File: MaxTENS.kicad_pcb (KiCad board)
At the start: 2 copper layers, 50.8 x 70.1 mm, 74 parts, among them IC1 ESP32-WROOM-32E-N8, J2 54-00170, J3 54-00170, J4 Conn_01x12, J5 20021121-00010C4LF, J6 Conn_01x02_Pin, Q1 PMV37ENEAR, Q16 NPN, Q17 PNP, Q18 NPN, Q19 NPN, Q2 NPN, Q20 PNP, Q21 NPN, Q3 NPN, Q4 NPN, Q5 PNP, Q6 NPN, Q7 NPN, Q8 PNP, Q9 NPN, U1 ADA4522-2ARMZ-R7, U2 MCP4232-503E/UN, U3 MCP73811T-420I/OT, U4 NCP176AMX330TCG

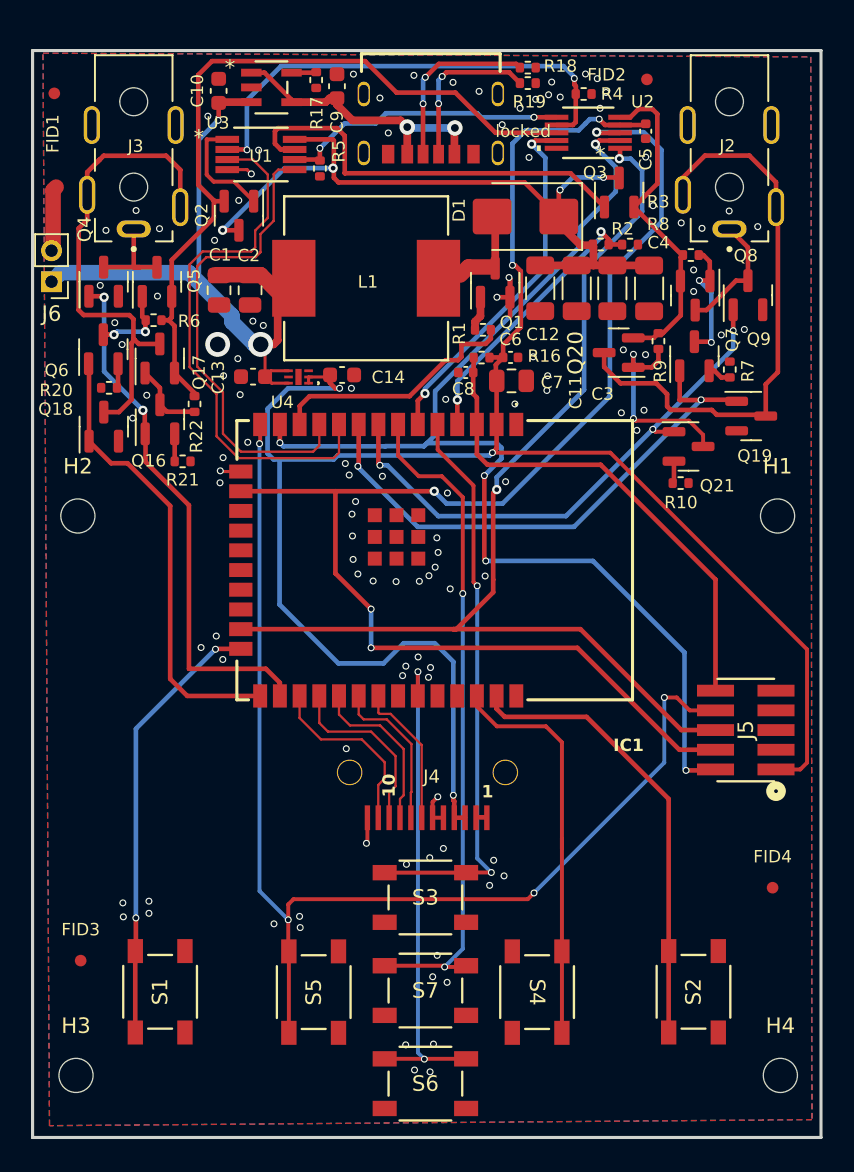
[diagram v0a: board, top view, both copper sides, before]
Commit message: version 2 with 0.8mm thickness
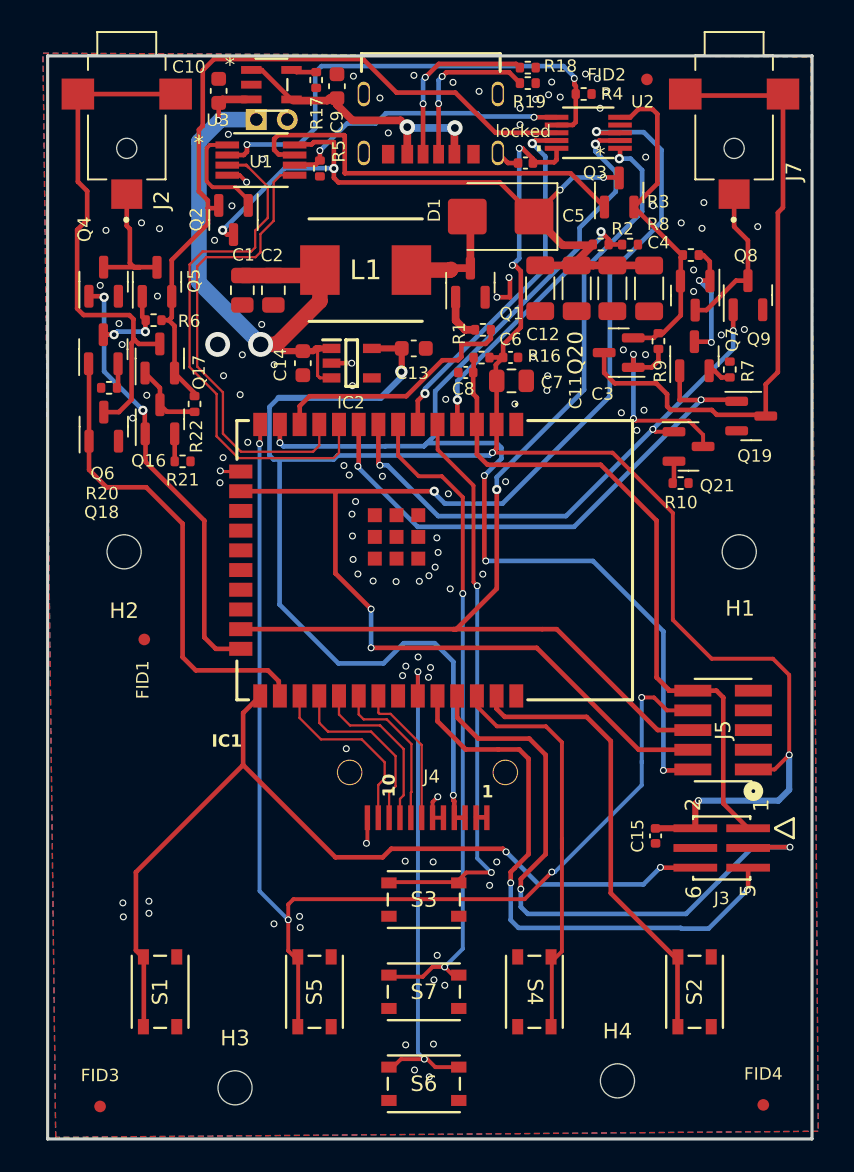
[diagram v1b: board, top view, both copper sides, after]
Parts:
- removed U4: NCP176AMX330TCG, Library:XDFN6_711AT_ONS
- added C15: 0.1u, Capacitor_SMD:C_0402_1005Metric, F.Cu at (238.0, 90.6)
- added IC2: AP7366-33W5-7, Library:SOT95P285X130-5N, F.Cu at (218.4, 60.1)
- added J7: PJ-040-SMT-TR, Library:CUI_PJ-040-SMT-TR, F.Cu at (243.1, 44.3)
- J2: value 54-00170 -> PJ-040-SMT-TR; footprint Library:TENSILITY_54-00170 -> Library:CUI_PJ-040-SMT-TR
- J3: value 54-00170 -> 20021121-00006C4LF; footprint Library:TENSILITY_54-00170 -> Library:CONN_20021121-00006C4LF_AMP
- J6: moved to B.Cu
- L1: value 33uH -> 10uH; footprint Library:IND_104CDM_SUM -> Library:INDPM7366X300N
- S1, S2, S3, S4, S5, S6, S7: value PTS647SM38SMTR2LFS -> PTS815 SJM 250 SMTR LFS; footprint Library:SW_PTS647SM38SMTR2LFS_CNK -> Library:SW4_PTS815 SJM 250 SMTR LFS_CNK
- moved J3 59.1 mm to (242.3, 91.4), turned to 90 degrees
- moved J2 38.9 mm to (203.9, 44.3), turned to -90 degrees
- moved FID1 35.7 mm to (205.1, 78.0)
- moved J6 16.8 mm to (212.3, 44.5), turned to -90 degrees
- moved FID4 14.0 mm to (245.0, 108.0)
- moved C13 10.5 mm to (222.4, 59.2), turned to 0 degrees
- moved H4 10.5 mm to (235.6, 106.4)
- moved H3 10.3 mm to (210.9, 106.9)
- moved FID3 9.48 mm to (202.2, 108.1)
- moved C5 8.02 mm to (229.7, 47.2), turned to 180 degrees
- moved H2 3.77 mm to (203.8, 72.3)
- moved H1 3.38 mm to (243.4, 72.3)
- moved C14 2.64 mm to (215.3, 60.1), turned to -90 degrees
- moved D1 1.60 mm to (228.1, 50.7)
- moved Q1 1.60 mm to (226.1, 55.0)
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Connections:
- C13 pad 1: +BATT -> +3.3V
- C14 pad 1: +3.3V -> +BATT
- IC1 pad 24: /MCU/CH1_BTN -> /ElectrodeChannels/CH1_1
- IC1 pad 25: /ElectrodeChannels/CH1_2 -> /MCU/CH1_BTN
- IC1 pad 26: /ElectrodeChannels/CH1_1 -> /ElectrodeChannels/CH1_2
- IC1 pad 34: unconnected-(IC1-RXD0-Pad34) -> /MCU/RXD
- IC1 pad 35: unconnected-(IC1-TXD0-Pad35) -> /MCU/TXD
- U2 pad 10: GND -> +3.3V
- U2 pad 4: +3.3V -> GND
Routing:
- net /MCU/TXD: track 0.00 -> 40.6 mm, vias 0 -> 2
- net /MCU/RXD: track 0.00 -> 37.3 mm, vias 0 -> 2
- net /MCU/CH1_BTN: track 28.5 -> 58.1 mm
- net +3.3V: track 126.6 -> 140.2 mm, vias 5 -> 7
- net /MCU/EN: track 32.2 -> 43.8 mm
- net /ElectrodeChannels/CH1_1: track 34.3 -> 28.3 mm
- net GND: track 17.3 -> 13.3 mm, vias 114 -> 109
- net /ElectrodeChannels/CH2_N: track 37.0 -> 40.8 mm
- net +BATT: track 50.4 -> 47.4 mm
- net /ElectrodeChannels/CH1_P: track 6.29 -> 8.72 mm
- net /ElectrodeChannels/CH2_P: track 8.01 -> 10.0 mm
- net Net-(D1-A): track 5.56 -> 7.26 mm
- net /MCU/CS: track 70.5 -> 69.0 mm
- net VCC: track 47.7 -> 49.1 mm
- net /ElectrodeChannels/CH1_2: track 29.4 -> 30.7 mm
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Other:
- board size 50.8 x 70.1 mm -> 49.3 x 69.8 mm

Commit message: v3: removed digital potentiometer, added 8 discrete resistors and one GPIO expander
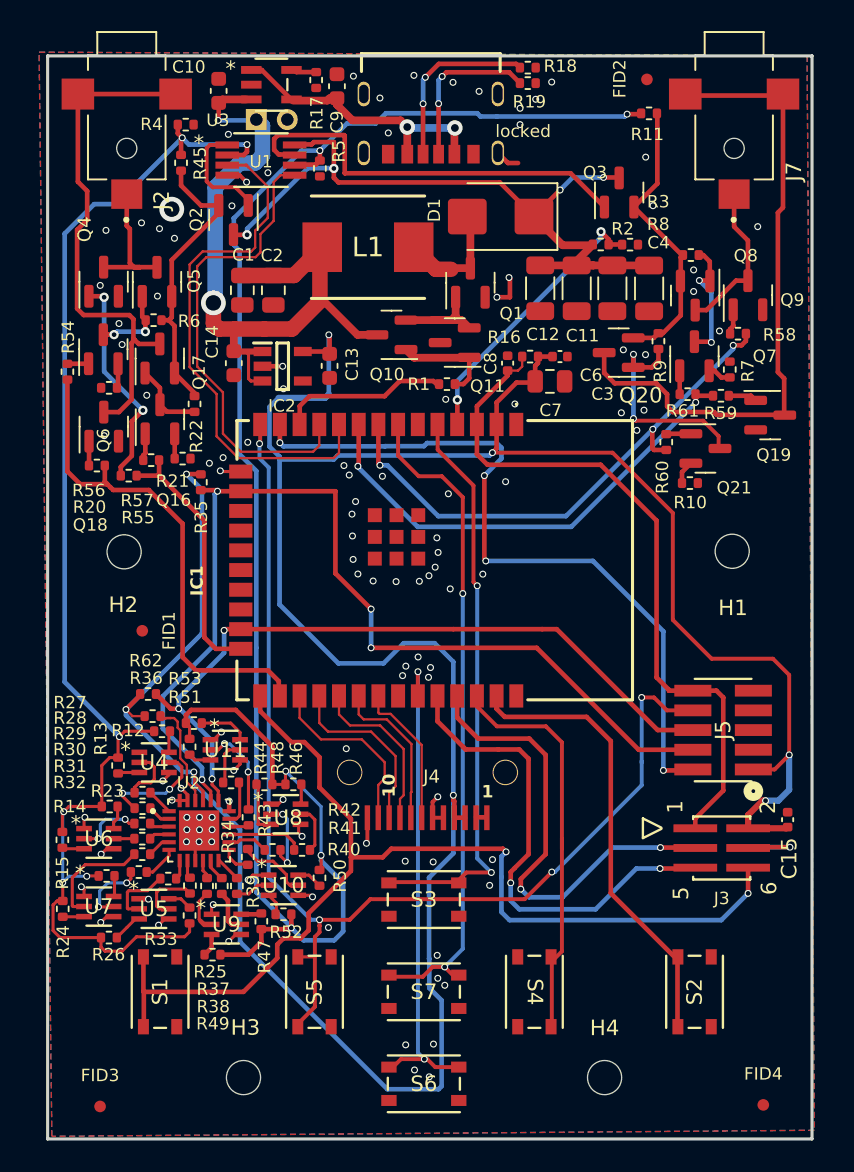
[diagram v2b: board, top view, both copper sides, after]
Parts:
- removed C5: 0.1u, Capacitor_SMD:C_0402_1005Metric
- added Q10: NPN, Package_TO_SOT_SMD:SOT-23, F.Cu at (221.0, 58.3)
- added Q11: PNP, Package_TO_SOT_SMD:SOT-23, F.Cu at (225.1, 58.8)
- added R11: 16k, Resistor_SMD:R_0402_1005Metric, F.Cu at (237.6, 44.0)
- added R12: 1M, Resistor_SMD:R_0402_1005Metric, F.Cu at (206.2, 83.9)
- added R13: 10k, Resistor_SMD:R_0402_1005Metric, F.Cu at (203.4, 86.1)
- added R14: 4.99k, Resistor_SMD:R_0402_1005Metric, F.Cu at (202.8, 88.7)
- added R15: 3.3k, Resistor_SMD:R_0402_1005Metric, F.Cu at (199.8, 90.9)
- added R23: 2.4k, Resistor_SMD:R_0402_1005Metric, F.Cu at (202.7, 93.2)
- added R24: 3.3k, Resistor_SMD:R_0402_1005Metric, F.Cu at (199.8, 95.3)
- added R25: 1.43k, Resistor_SMD:R_0402_1005Metric, F.Cu at (208.0, 95.8)
- added R26: 1.1k, Resistor_SMD:R_0402_1005Metric, F.Cu at (202.8, 97.2)
- added R27: 510, Resistor_SMD:R_0402_1005Metric, F.Cu at (205.0, 87.8)
- added R28: 510, Resistor_SMD:R_0402_1005Metric, F.Cu at (205.0, 88.8)
- added R29: 510, Resistor_SMD:R_0402_1005Metric, F.Cu at (204.9, 89.8)
- added R30: 510, Resistor_SMD:R_0402_1005Metric, F.Cu at (204.9, 90.8)
- added R31: 510, Resistor_SMD:R_0402_1005Metric, F.Cu at (204.9, 91.8)
- added R32: 510, Resistor_SMD:R_0402_1005Metric, F.Cu at (204.7, 93.0)
- added R33: 510, Resistor_SMD:R_0402_1005Metric, F.Cu at (206.6, 93.4)
- added R34: 510, Resistor_SMD:R_0402_1005Metric, F.Cu at (208.0, 93.8)
- added R35: 10k, Resistor_SMD:R_0402_1005Metric, F.Cu at (208.7, 67.8)
- added R36: 10k, Resistor_SMD:R_0402_1005Metric, F.Cu at (205.3, 81.5)
- added R37: 510, Resistor_SMD:R_0402_1005Metric, F.Cu at (209.1, 93.8)
- added R38: 510, Resistor_SMD:R_0402_1005Metric, F.Cu at (210.1, 93.8)
- added R39: 510, Resistor_SMD:R_0402_1005Metric, F.Cu at (211.1, 93.8)
- added R40: 510, Resistor_SMD:R_0402_1005Metric, F.Cu at (211.8, 92.0)
- added R41: 510, Resistor_SMD:R_0402_1005Metric, F.Cu at (213.3, 91.5)
- added R42: 510, Resistor_SMD:R_0402_1005Metric, F.Cu at (215.2, 91.5)
- added R43: 510, Resistor_SMD:R_0402_1005Metric, F.Cu at (211.8, 89.4)
- added R44: 510, Resistor_SMD:R_0402_1005Metric, F.Cu at (210.7, 87.2)
- added R45: 16k, Resistor_SMD:R_0402_1005Metric, F.Cu at (207.4, 47.2)
- added R46: 2.4k, Resistor_SMD:R_0402_1005Metric, F.Cu at (214.7, 87.3)
- added R47: 1M, Resistor_SMD:R_0402_1005Metric, F.Cu at (212.6, 96.1)
- added R48: 3.3k, Resistor_SMD:R_0402_1005Metric, F.Cu at (212.8, 87.3)
- added R49: 10k, Resistor_SMD:R_0402_1005Metric, F.Cu at (209.5, 98.3)
- added R50: 4.99k, Resistor_SMD:R_0402_1005Metric, F.Cu at (216.4, 93.3)
- added R51: 1.43k, Resistor_SMD:R_0402_1005Metric, F.Cu at (208.3, 83.3)
- added R52: 3.3k, Resistor_SMD:R_0402_1005Metric, F.Cu at (214.1, 95.7)
- added R53: 1.1k, Resistor_SMD:R_0402_1005Metric, F.Cu at (208.0, 84.9)
- added R54: 300, Resistor_SMD:R_0402_1005Metric, F.Cu at (200.1, 60.7)
- added R55: 300, Resistor_SMD:R_0402_1005Metric, F.Cu at (204.1, 67.4)
- added R56: 300, Resistor_SMD:R_0402_1005Metric, F.Cu at (202.0, 66.8)
- added R57: 300, Resistor_SMD:R_0402_1005Metric, F.Cu at (205.5, 66.4)
- added R58: 300, Resistor_SMD:R_0402_1005Metric, F.Cu at (243.3, 58.2)
- added R59: 300, Resistor_SMD:R_0402_1005Metric, F.Cu at (242.2, 62.2)
- added R60: 300, Resistor_SMD:R_0402_1005Metric, F.Cu at (238.7, 65.2)
- added R61: 300, Resistor_SMD:R_0402_1005Metric, F.Cu at (240.1, 62.1)
- added R62: 10k, Resistor_SMD:R_0402_1005Metric, F.Cu at (205.6, 82.9)
- added U10: 2N7002KDW_R1_00001, Library:SOT-363-6_2P2X1P35_ONS, F.Cu at (214.1, 93.8)
- added U11: 2N7002KDW_R1_00001, Library:SOT-363-6_2P2X1P35_ONS, F.Cu at (210.3, 85.1)
- added U4: 2N7002KDW_R1_00001, Library:SOT-363-6_2P2X1P35_ONS, F.Cu at (205.7, 85.9)
- added U5: 2N7002KDW_R1_00001, Library:SOT-363-6_2P2X1P35_ONS, F.Cu at (205.7, 95.3)
- added U6: 2N7002KDW_R1_00001, Library:SOT-363-6_2P2X1P35_ONS, F.Cu at (202.2, 90.8)
- added U7: 2N7002KDW_R1_00001, Library:SOT-363-6_2P2X1P35_ONS, F.Cu at (202.2, 95.2)
- added U8: 2N7002KDW_R1_00001, Library:SOT-363-6_2P2X1P35_ONS, F.Cu at (214.2, 89.2)
- added U9: 2N7002KDW_R1_00001, Library:SOT-363-6_2P2X1P35_ONS, F.Cu at (210.4, 96.3)
- L1: value 10uH -> 22uH
- R1: value 0 -> 100
- R5: value 1k -> 30k
- U2: value MCP4232-503E/UN -> TCA9535RTWR; footprint Library:MSOP10_MC_MCH -> Library:QFN50P400X400X80-25N
- moved U2 51.5 mm to (208.6, 90.3), turned to 0 degrees
- moved R4 25.7 mm to (207.8, 44.8)
- moved C15 8.58 mm to (246.6, 89.6), turned to -90 degrees
- moved C13 5.54 mm to (217.0, 60.3), turned to -90 degrees
- moved IC2 4.45 mm to (214.0, 60.4)
- moved C14 4.45 mm to (210.8, 60.1)
- moved R1 4.20 mm to (224.6, 61.5), turned to 0 degrees
- moved C6 3.19 mm to (231.9, 59.7)
- moved R16 3.13 mm to (229.9, 59.7)
- moved C8 2.77 mm to (228.5, 60.1), turned to 90 degrees
- moved C7 2.48 mm to (231.2, 61.3)
- moved L1 1.48 mm to (219.5, 52.7)
- moved Q19 1.23 mm to (245.4, 63.5)
- moved Q21 1.10 mm to (241.2, 65.7)
- moved H4 0.86 mm to (234.8, 106.2)
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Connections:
- IC1 pad 23: /MCU/CS -> /Opamp/SCL
- J3 pad 1: /MCU/EN -> +3.3V
- J3 pad 2: +3.3V -> /MCU/EN
- J3 pad 3: /MCU/TXD -> GND
- J3 pad 4: GND -> /MCU/TXD
- J3 pad 5: /MCU/RXD -> /MCU/CH1_BTN
- J3 pad 6: /MCU/CH1_BTN -> /MCU/RXD
- J5 pad 6: /MCU/CS -> /Opamp/SCL
- Q16 pad 1: /ElectrodeChannels/CH1_1 -> Net-(Q16-B)
- Q18 pad 1: /ElectrodeChannels/CH1_2 -> Net-(Q18-B)
- Q19 pad 1: /ElectrodeChannels/CH2_2 -> Net-(Q19-B)
- Q21 pad 1: /ElectrodeChannels/CH2_1 -> Net-(Q21-B)
- Q4 pad 1: /ElectrodeChannels/CH1_1 -> Net-(Q4-B)
- Q6 pad 1: /ElectrodeChannels/CH1_2 -> Net-(Q6-B)
- Q7 pad 1: /ElectrodeChannels/CH2_2 -> Net-(Q7-B)
- Q9 pad 1: /ElectrodeChannels/CH2_1 -> Net-(Q9-B)
- R1 pad 2: Net-(Q1-G) -> Net-(Q10-B)
- U2 pad 1: /MCU/CS -> Net-(U2-P00)
- U2 pad 10: +3.3V -> Net-(U2-P10)
- U2 pad 2: /MCU/SCLK -> Net-(U2-P01)
- U2 pad 3: /MCU/MOSI -> Net-(U2-P02)
- U2 pad 4: GND -> Net-(U2-P03)
- U2 pad 5: +OUT_2 -> Net-(U2-P04)
- U2 pad 6: /Opamp/P1W -> Net-(U2-P05)
- U2 pad 7: /Opamp/P0W -> Net-(U2-P06)
- U2 pad 8: +OUT_1 -> Net-(U2-P07)
- U2 pad 9: /MCU/MISO -> GND
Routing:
- net /Opamp/P1W: track 18.7 -> 114.7 mm, vias 2 -> 5
- net /MCU/CS: track 69.0 -> 0.00 mm, vias 2 -> 0
- net +3.3V: track 140.2 -> 196.1 mm, vias 7 -> 8
- net /Opamp/P0W: track 31.7 -> 85.3 mm, vias 2 -> 6
- net /Opamp/SCL: track 0.00 -> 48.1 mm, vias 0 -> 3
- net +OUT_1: track 49.4 -> 18.7 mm
- net /MCU/SCLK: track 74.6 -> 47.8 mm, vias 5 -> 4
- net /MCU/MISO: track 23.5 -> 0.00 mm, vias 2 -> 0
- net GND: track 13.3 -> 36.3 mm, vias 109 -> 113
- net /MCU/MOSI: track 85.0 -> 65.9 mm
- net Net-(Q4-B): track 0.00 -> 14.1 mm, vias 0 -> 2
- net /ElectrodeChannels/CH1_1: track 28.3 -> 16.7 mm, vias 2 -> 0
- net /MCU/CH1_BTN: track 58.1 -> 69.2 mm
- net /MCU/TXD: track 40.6 -> 30.2 mm
- net /Opamp/P025: track 0.00 -> 7.22 mm
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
